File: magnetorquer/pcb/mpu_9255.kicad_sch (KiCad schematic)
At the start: 1 part

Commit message: feat: upload all changes for sch
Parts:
- renumbered U4 to U2
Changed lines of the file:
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@@
 		(dnp no)
 		(fields_autoplaced yes)
-		(property "Reference" "U4"
+		(property "Reference" "U2"
 			(at 127 54.61 0)
 			(effects
@@
 		(pin "1"
 		)
+		(instances
+			(project "mag"
+				(path "/14c04de7-71ee-4f20-9e6e-041dbb035733/cff9f0de-66a8-40e0-bfeb-91cf114478e3"
+					(reference "U2")
+					(unit 1)
+				)
+			)
+		)
 	)
 	(symbol
@@
 		(dnp no)
 		(fields_autoplaced yes)
-		(property "Reference" "#PWR018"
+		(property "Reference" "#PWR0102"
 			(at 110.49 91.44 0)
 			(effects
@@
 		(pin "1"
 		)
+		(instances
+			(project "mag"
+				(path "/14c04de7-71ee-4f20-9e6e-041dbb035733/cff9f0de-66a8-40e0-bfeb-91cf114478e3"
+					(reference "#PWR0102")
+					(unit 1)
+				)
+			)
+		)
 	)
 	(symbol
@@
 		(dnp no)
 		(fields_autoplaced yes)
-		(property "Reference" "#PWR016"
+		(property "Reference" "#PWR0101"
 			(at 110.49 63.5 0)
 			(effects
@@
 		(pin "1"
 		)
+		(instances
+			(project "mag"
+				(path "/14c04de7-71ee-4f20-9e6e-041dbb035733/cff9f0de-66a8-40e0-bfeb-91cf114478e3"
+					(reference "#PWR0101")
+					(unit 1)
+				)
+			)
+		)
 	)

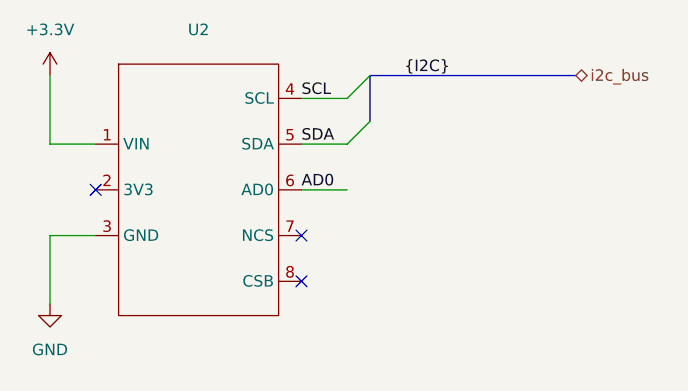
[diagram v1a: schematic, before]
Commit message: start routing pcb
It needs a power regulator and a battery terminal
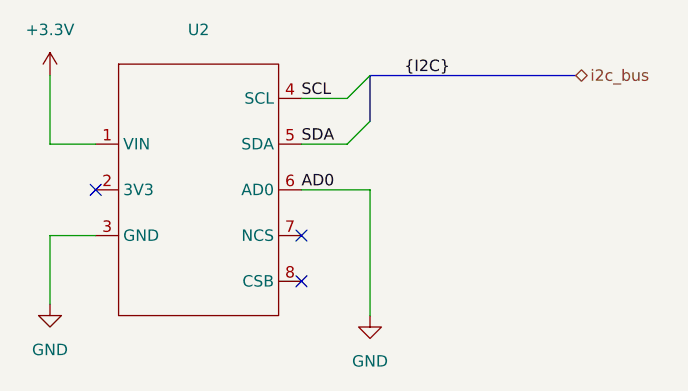
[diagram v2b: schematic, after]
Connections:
- net AD0 is gone; now on net GND: U2.6 (AD0)
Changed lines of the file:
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@@
+		)
+	)
+	(wire
+		(pts
+			(xy 146.05 86.36) (xy 146.05 72.39)
+		)
+		(stroke
+			(width 0)
+			(type default)
+		)
+	)
+	(wire
+		(pts
+			(xy 146.05 72.39) (xy 138.43 72.39)
+		)
+		(stroke
+			(width 0)
+			(type default)
 		)
 	)
@@
 		(pts
 			(xy 143.51 67.31) (xy 138.43 67.31)
-		)
-		(stroke
-			(width 0)
-			(type default)
-		)
-	)
-	(wire
-		(pts
-			(xy 138.43 72.39) (xy 143.51 72.39)
 		)
 		(stroke
@@
 					(unit 1)
 				)
+			)
+		)
+	)
+	(symbol
+		(lib_id "power:GND")
+		(at 146.05 86.36 0)
+		(unit 1)
+		(exclude_from_sim no)
+		(in_bom yes)
+		(on_board yes)
+		(dnp no)
+		(fields_autoplaced yes)
+		(property "Reference" "#PWR09"
+			(at 146.05 92.71 0)
+			(effects
+				(font
+					(size 1.27 1.27)
+				)
+				(hide yes)
+			)
+		)
+		(property "Value" "GND"
+			(at 146.05 91.44 0)
+			(effects
+				(font
+					(size 1.27 1.27)
+				)
+			)
+		)
+		(property "Footprint" ""
+			(at 146.05 86.36 0)
+			(effects
+				(font
+					(size 1.27 1.27)
+				)
+				(hide yes)
+			)
+		)
+		(property "Datasheet" ""
+			(at 146.05 86.36 0)
+			(effects
+				(font
+					(size 1.27 1.27)
+				)
+				(hide yes)
+			)
+		)
+		(property "Description" "Power symbol creates a global label with name \"GND\" , ground"
+			(at 146.05 86.36 0)
+			(effects
+				(font
+					(size 1.27 1.27)
+				)
+				(hide yes)
+			)
+		)
+		(pin "1"
+		)
+		(instances
+			(project ""
+				(path "/14c04de7-71ee-4f20-9e6e-041dbb035733/cff9f0de-66a8-40e0-bfeb-91cf114478e3"
+					(reference "#PWR09")
+					(unit 1)
+				)
